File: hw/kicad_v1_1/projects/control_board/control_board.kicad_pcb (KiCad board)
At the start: 2 copper layers, 100 x 50 mm, 73 parts, among them CON1 161-0725-E, IC1 ATMEGA168A-A, P1 CONN_02X12_isolate_hv, P2 CONN_02X06, P3 CONN_02X05, P4 CONN_01X01, P5 CONN_01X01, P6 CONN_01X01, P7 CONN_01X01, Q1 IPB50R199CP, SW1 SW_LPH_PUSH, SW2 SW_LPH_PUSH, SW3 SW_LPH_PUSH, SW4 SW_LPH_PUSH, U1 MAX1771, U2 MCP7940N, U3 74HC595, U4 74HC595, U5 TPS563208, Y1 32.768kHz

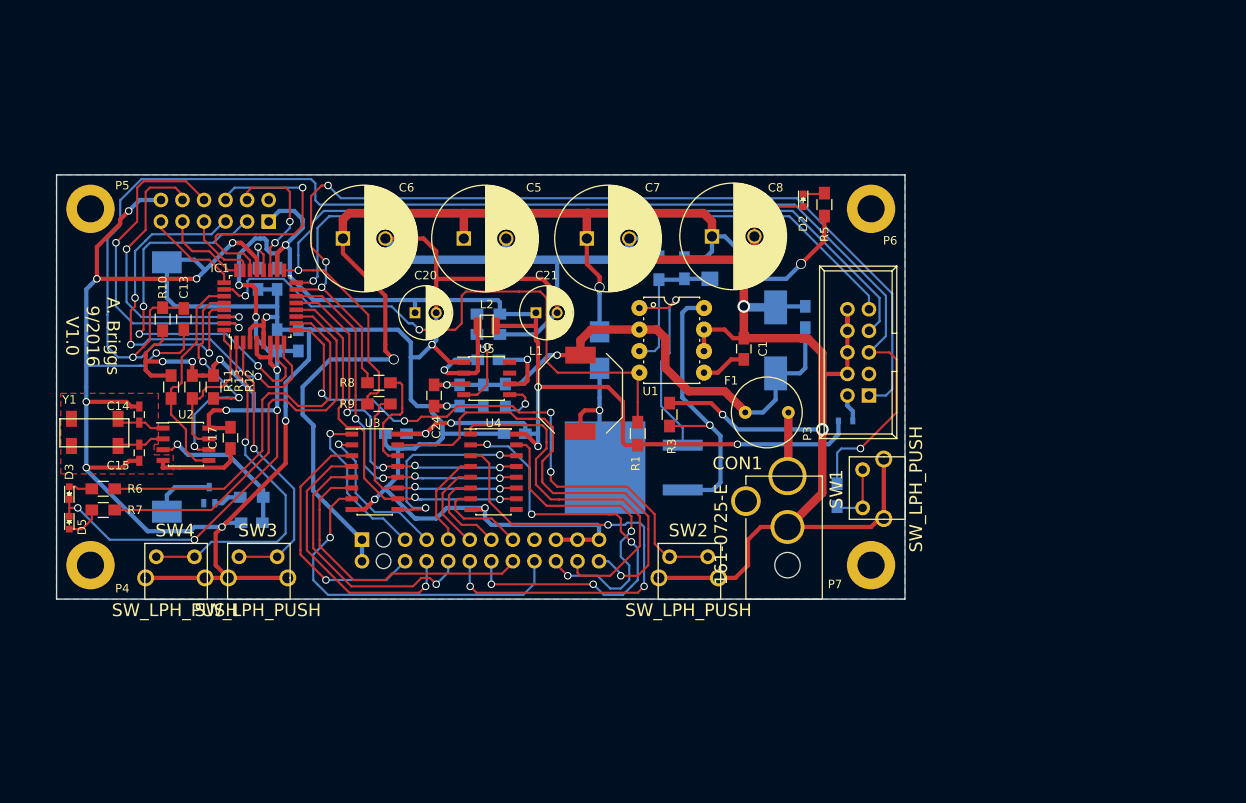
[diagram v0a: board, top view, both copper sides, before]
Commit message: Updates to BOM
Start to update BOM for 180V supply
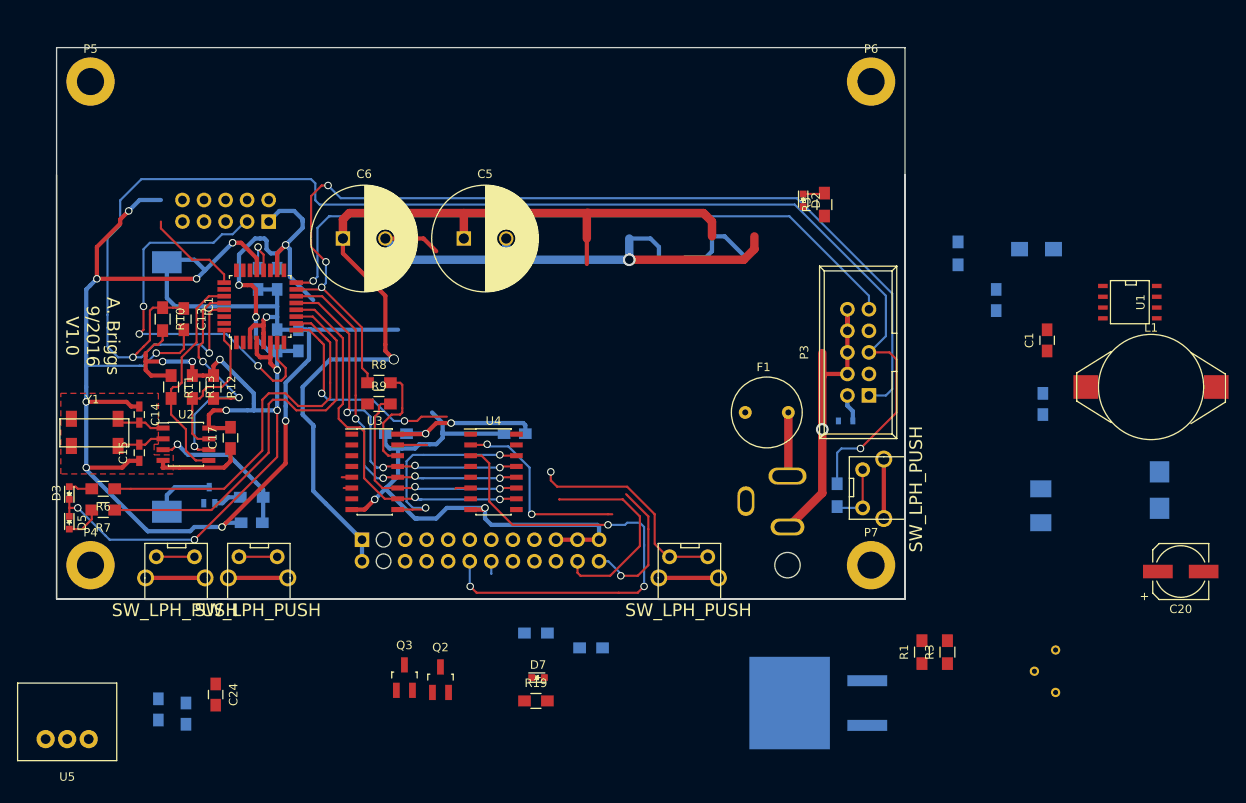
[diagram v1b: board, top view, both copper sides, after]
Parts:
- removed C21: 22uF, Capacitors_ThroughHole:C_Radial_D6.3_L11.2_P2.5
- removed C25: 0.1uF, Capacitors_SMD:C_0805_HandSoldering
- removed C7, C8: 47uF, Capacitors_ThroughHole:C_Radial_D12.5_L25_P5
- removed L2: LBR2518T2R2M, Nixie:ind_2518
- added D7: LTST-C190GKT, LEDs:LED_0603, F.Cu at (171.2, 129.2)
- added Q2: MMBTA42, TO_SOT_Packages_SMD:SOT-23_Handsoldering, F.Cu at (159.8, 129.5)
- added Q3: MMBTA42, TO_SOT_Packages_SMD:SOT-23_Handsoldering, F.Cu at (155.5, 129.2)
- added R19: 330, Resistors_SMD:R_0805_HandSoldering, F.Cu at (171.0, 132.0)
- C2: value 68uF -> 10uF; footprint Capacitors_Tantalum_SMD:TantalC_SizeD_EIA-7343_HandSoldering -> Capacitors_SMD:C_1210_HandSoldering
- C20: value 22uF -> 100uF; footprint Capacitors_ThroughHole:C_Radial_D6.3_L11.2_P2.5 -> Capacitors_SMD:c_elec_6.3x7.7
- CON1: moved to B.Cu
- L1: value 150u -> 100u; footprint Nixie:SRU1048-151Y -> Nixie:B82479A1104M
- P2: value CONN_02X06 -> CONN_02X05; footprint Pin_Headers:Pin_Header_Straight_2x06 -> Pin_Headers:Pin_Header_Straight_2x05
- R15: value 10k -> 4.7k
- R16: value 10k -> RVAR-TRIM; footprint Resistors_SMD:R_0805_HandSoldering -> Nixie:67ZR5KLF
- R17: value 33.2k -> 470k
- R3: value 0.1 -> 0.05
- R4: value 1.123MEG -> 1.5MEG
- R5: value 18k -> 1.5k
- R6, R7: value 100 -> 330
- U1: footprint Power_Integrations:PDIP-8 -> SMD_Packages:SOIC-8-N
- U5: value TPS563208 -> R-78E5.0-0.5; footprint Housings_SOIC:SOIC-8_3.9x4.9mm_Pitch1.27mm -> Nixie:R-78E5.0-0.5
- moved C20 95.3 mm to (247.0, 116.8)
- moved R16 72.5 mm to (232.2, 128.5)
- moved D1 68.0 mm to (244.5, 103.8)
- moved L1 67.3 mm to (243.5, 95.0), turned to 0 degrees
- moved U5 65.2 mm to (115.8, 136.5)
- moved U1 54.2 mm to (241.0, 85.0)
- moved C23 53.3 mm to (126.5, 133.0)
- moved C22 49.5 mm to (129.8, 133.5)
- moved C24 43.7 mm to (133.2, 131.2)
- moved R3 43.1 mm to (219.5, 126.2)
- moved R1 42.3 mm to (216.5, 126.2)
- moved R15 38.9 mm to (177.5, 125.8)
- moved R17 38.0 mm to (171.0, 124.0)
- moved C4 36.9 mm to (225.2, 84.8)
- moved C2 36.8 mm to (230.5, 109.0)
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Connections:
- net /MCU/SEL_DOT_BOT renamed /MCU/SEL_N2_D
- C10 pad 1: +3V3 -> +5V
- C11 pad 1: +3V3 -> +5V
- C17 pad 2: +3V3 -> +5V
- C18 pad 1: +3V3 -> +5V
- C19 pad 1: +3V3 -> +5V
- C20 pad 1: +3V3 -> +12V
- C22 pad 1: +12V -> +5V
- C4 pad 2: +170V -> +180V
- C5 pad 1: +170V -> +180V
- C6 pad 1: +170V -> +180V
- C9 pad 1: +3V3 -> +5V
- CON1 pad 2: Net-(CON1-Pad2) -> (no net)
- D1 pad 1: +170V -> +180V
- D2 pad 2: GND -> Net-(D2-Pad2)
- D3 pad 1: +3V3 -> +5V
- D4 pad 2: +3V3 -> +5V
- D5 pad 1: +3V3 -> +5V
- D6 pad 2: Net-(D6-Pad2) -> (no net)
- IC1 pad 18: +3V3 -> +5V
- IC1 pad 26: /Nixie Power Supply/180V_SHDN -> /MCU/180V_EN
- IC1 pad 4: +3V3 -> +5V
- IC1 pad 6: +3V3 -> +5V
- IC1 pad 8: /MCU/CYA1 -> /MCU/COL_SEL
- P1 pad 1: +170V -> +180V
- P1 pad 10: /MCU/SEL_FIVE -> /MCU/SEL_N2_C
- P1 pad 11: /MCU/SEL_NIX1 -> /MCU/SEL_N3_D
- P1 pad 13: /MCU/SEL_NIX2 -> /MCU/SEL_N0_A
- P1 pad 14: /MCU/SEL_DOT_TOP -> /MCU/SEL_N1_A
- P1 pad 15: /MCU/SEL_NIX3 -> /MCU/SEL_N0_B
- P1 pad 16: /MCU/SEL_SIX -> /MCU/SEL_N1_B
- P1 pad 17: Net-(P1-Pad17) -> /MCU/SEL_N0_C
- P1 pad 18: /MCU/SEL_SEVEN -> /MCU/SEL_N1_C
- P1 pad 19: GND -> /MCU/SEL_N0_D
- P1 pad 2: +170V -> +180V
- P1 pad 20: /MCU/SEL_EIGHT -> /MCU/SEL_N1_D
- P1 pad 21: GND -> +5V
- P1 pad 22: /MCU/SEL_NINE -> /MCU/COL_SEL
- P1 pad 24: /MCU/SEL_ZERO -> GND
- P1 pad 5: /MCU/SEL_ONE -> /MCU/SEL_N3_A
- P1 pad 6: /MCU/SEL_THREE -> /MCU/SEL_N2_A
- P1 pad 7: /MCU/SEL_TWO -> /MCU/SEL_N3_B
- P1 pad 8: /MCU/SEL_FOUR -> /MCU/SEL_N2_B
- P1 pad 9: /MCU/SEL_NIX0 -> /MCU/SEL_N3_C
- P2 pad 1: +3V3 -> +5V
- P2 pad 10: /MCU/CYA5 -> GND
- P2 pad 2: Net-(P2-Pad2) -> /MCU/CYA7
- P2 pad 4: /MCU/CYA7 -> /MCU/CYA8
- P2 pad 5: /MCU/CYA1 -> /MCU/CYA2
- P2 pad 6: /MCU/CYA8 -> /MCU/CYA6
- P2 pad 7: /MCU/CYA2 -> /MCU/CYA3
- P2 pad 8: /MCU/CYA6 -> /MCU/CYA5
- P2 pad 9: /MCU/CYA3 -> /MCU/CYA4
- P3 pad 3: Net-(P3-Pad3) -> (no net)
- P4 pad 1: Net-(P4-Pad1) -> (no net)
- P5 pad 1: Net-(P5-Pad1) -> (no net)
- P6 pad 1: Net-(P6-Pad1) -> (no net)
- P7 pad 1: Net-(P7-Pad1) -> (no net)
- R1 pad 1: +3V3 -> +12V
- R1 pad 2: /Nixie Power Supply/180V_SHDN -> Net-(Q2-Pad3)
- R10 pad 2: +3V3 -> +5V
- R11 pad 1: +3V3 -> +5V
- R12 pad 1: +3V3 -> +5V
- R13 pad 1: +3V3 -> +5V
- R15 pad 1: GND -> Net-(Q2-Pad1)
- R15 pad 2: Net-(R15-Pad2) -> /MCU/180V_EN
- R16 pad 1: Net-(R16-Pad1) -> Net-(C4-Pad1)
- R16 pad 2: +12V -> Net-(R16-Pad2)
- R17 pad 1: +3V3 -> Net-(Q3-Pad1)
- R17 pad 2: Net-(R15-Pad2) -> +180V
- R2 pad 1: Net-(C4-Pad1) -> Net-(R16-Pad2)
- R4 pad 2: +170V -> +180V
- R5 pad 1: +170V -> +12V
- SW1 pad 2: GND -> Net-(R18-Pad1)
- SW1 pad 3: Net-(R18-Pad1) -> (no net)
- SW1 pad 4: Net-(R18-Pad1) -> GND
- SW2 pad 2: GND -> Net-(IC1-Pad9)
- SW2 pad 3: Net-(IC1-Pad9) -> (no net)
- SW2 pad 4: Net-(IC1-Pad9) -> GND
- SW3 pad 2: GND -> Net-(IC1-Pad2)
- SW3 pad 3: Net-(IC1-Pad2) -> (no net)
- SW3 pad 4: Net-(IC1-Pad2) -> GND
- SW4 pad 2: GND -> Net-(IC1-Pad1)
- SW4 pad 3: Net-(IC1-Pad1) -> (no net)
- SW4 pad 4: Net-(IC1-Pad1) -> GND
- U1 pad 4: /Nixie Power Supply/180V_SHDN -> Net-(Q2-Pad3)
- U2 pad 8: +3V3 -> +5V
- U3 pad 1: /MCU/SEL_ONE -> /MCU/SEL_N0_B
- U3 pad 15: /MCU/SEL_ZERO -> /MCU/SEL_N0_A
- U3 pad 16: +3V3 -> +5V
- U3 pad 2: /MCU/SEL_TWO -> /MCU/SEL_N0_C
- U3 pad 3: /MCU/SEL_THREE -> /MCU/SEL_N0_D
- U3 pad 4: /MCU/SEL_FOUR -> /MCU/SEL_N1_A
- U3 pad 5: /MCU/SEL_FIVE -> /MCU/SEL_N1_B
- U3 pad 6: /MCU/SEL_SIX -> /MCU/SEL_N1_C
- U3 pad 7: /MCU/SEL_SEVEN -> /MCU/SEL_N1_D
- U4 pad 1: /MCU/SEL_NINE -> /MCU/SEL_N2_B
- U4 pad 15: /MCU/SEL_EIGHT -> /MCU/SEL_N2_A
- U4 pad 16: +3V3 -> +5V
- U4 pad 2: /MCU/SEL_DOT_TOP -> /MCU/SEL_N2_C
- U4 pad 4: /MCU/SEL_NIX0 -> /MCU/SEL_N3_A
- U4 pad 5: /MCU/SEL_NIX1 -> /MCU/SEL_N3_B
- U4 pad 6: /MCU/SEL_NIX2 -> /MCU/SEL_N3_C
- U4 pad 7: /MCU/SEL_NIX3 -> /MCU/SEL_N3_D
- U4 pad 9: Net-(U4-Pad9) -> (no net)
- U5 pad 1: GND -> +12V
- U5 pad 2: Net-(C25-Pad2) -> GND
- U5 pad 3: +12V -> +5V
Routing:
- net +3V3: track 257.5 -> 0.00 mm, vias 16 -> 0
- net GND: track 564.9 -> 394.2 mm, vias 18 -> 15
- net +5V: track 0.00 -> 161.0 mm, vias 0 -> 13
- net +170V: track 146.6 -> 0.00 mm, vias 3 -> 0
- net +180V: track 0.00 -> 110.7 mm, vias 0 -> 1
- net Net-(IC1-Pad17): track 106.6 -> 0.12 mm, vias 1 -> 0
- net /Nixie Power Supply/180V_SHDN: track 71.6 -> 0.00 mm, vias 2 -> 0
- net +12V: track 64.7 -> 0.00 mm, vias 2 -> 0
- net /MCU/SEL_ZERO: track 56.4 -> 0.00 mm, vias 1 -> 0
- net /MCU/SEL_DOT_TOP: track 54.2 -> 0.00 mm, vias 5 -> 0
- net /MCU/CYA1: track 50.0 -> 0.00 mm, vias 3 -> 0
- net /MCU/SEL_NINE: track 44.7 -> 0.00 mm
- net /MCU/SEL_SEVEN: track 42.3 -> 0.00 mm, vias 1 -> 0
- net /MCU/CYA6: track 41.7 -> 0.38 mm, vias 2 -> 0
- net /MCU/SEL_EIGHT: track 38.8 -> 0.00 mm, vias 2 -> 0
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- removed copper zone on B.Cu, net GND
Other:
- board size 100 x 50 mm -> 100 x 65 mm

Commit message: Complete with errors
Check in before moving header. Currently the headers don't match up. If
I'm going to connect them with standard header I need to move it
significantly. Check in as a roll back point.
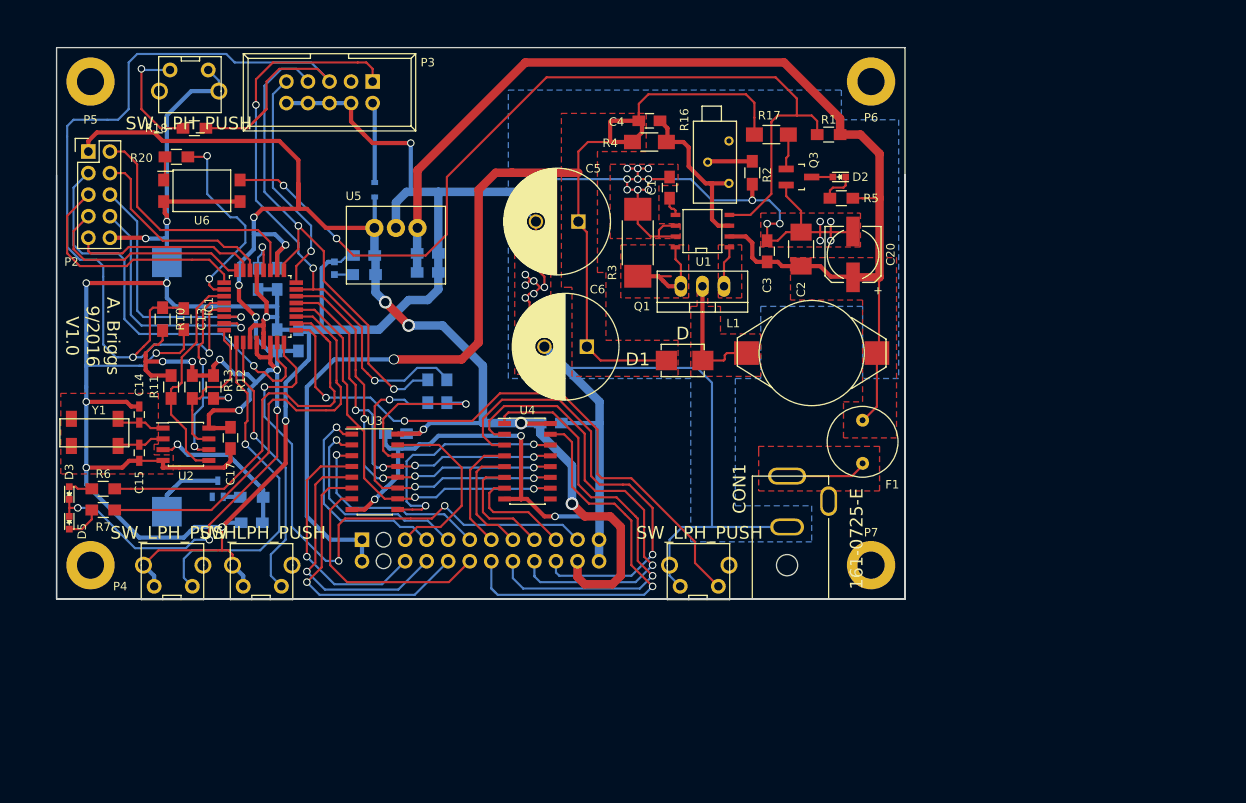
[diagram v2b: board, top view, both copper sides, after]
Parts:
- removed Q2: MMBTA42, TO_SOT_Packages_SMD:SOT-23_Handsoldering
- removed R15: 4.7k, Resistors_SMD:R_0805_HandSoldering
- added R20: 1k, Resistors_SMD:R_0805_HandSoldering, F.Cu at (128.6, 67.9)
- added U6: LTV-817, Opto-Devices:Optocoupler_SMD_LTV-817S, F.Cu at (131.6, 71.9)
- C2, C3, C4, CON1, D1, P2, R16, R18, R2, R4: moved to F.Cu
- C24, D7, R19, R8, R9: moved to B.Cu
- Q1: value IPB50R199CP -> IRF644PBF; footprint Nixie:to263 -> TO_SOT_Packages_THT:TO-220_Neutral123_Vertical; moved to F.Cu
- R17: footprint Resistors_SMD:R_0805_HandSoldering -> Resistors_SMD:R_1206_HandSoldering; moved to F.Cu
- R3: footprint Resistors_SMD:R_0805_HandSoldering -> Resistors_SMD:R_2512_HandSoldering
- moved SW1 91.3 mm to (132.4, 60.1), turned to 180 degrees
- moved R18 87.2 mm to (130.8, 64.5), turned to 0 degrees
- moved Q3 75.1 mm to (202.0, 70.2), turned to 270 degrees
- moved U5 71.6 mm to (154.5, 76.2), turned to 180 degrees
- moved R16 71.3 mm to (193.8, 68.5), turned to 270 degrees
- moved P3 69.2 mm to (151.8, 59.0), turned to 180 degrees
- moved R17 65.0 mm to (198.8, 65.2)
- moved R1 62.0 mm to (205.5, 65.2), turned to 180 degrees
- moved D4 61.8 mm to (152.0, 71.8), turned to 270 degrees
- moved D1 60.6 mm to (185.1, 91.9), turned to 0 degrees
- moved R3 60.5 mm to (183.0, 78.0)
- moved C23 60.5 mm to (158.2, 81.5), turned to 0 degrees
- moved C22 57.9 mm to (150.8, 79.5), turned to 180 degrees
- moved C24 57.7 mm to (158.2, 79.2), turned to 0 degrees
- moved R19 54.2 mm to (150.8, 81.8), turned to 180 degrees
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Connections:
- net Net-(Q2-Pad3) renamed /MCU/180V_SHDN
- IC1 pad 23: /MCU/CYA2 -> /MCU/CYA4
- IC1 pad 25: /MCU/CYA4 -> /MCU/CYA2
- IC1 pad 30: /MCU/CYA5 -> /MCU/CYA6
- IC1 pad 31: /MCU/CYA6 -> /MCU/CYA5
- IC1 pad 8: /MCU/COL_SEL -> /SEL_COL
- P1 pad 10: /MCU/SEL_N2_C -> /SEL_N3_C
- P1 pad 11: /MCU/SEL_N3_D -> /SEL_N2_D
- P1 pad 12: /MCU/SEL_N2_D -> /SEL_N3_D
- P1 pad 13: /MCU/SEL_N0_A -> /SEL_N1_A
- P1 pad 14: /MCU/SEL_N1_A -> /SEL_N0_A
- P1 pad 15: /MCU/SEL_N0_B -> /SEL_N1_B
- P1 pad 16: /MCU/SEL_N1_B -> /SEL_N0_B
- P1 pad 17: /MCU/SEL_N0_C -> /SEL_N1_C
- P1 pad 18: /MCU/SEL_N1_C -> /SEL_N0_C
- P1 pad 19: /MCU/SEL_N0_D -> /SEL_N1_D
- P1 pad 20: /MCU/SEL_N1_D -> /SEL_N0_D
- P1 pad 21: +5V -> /SEL_COL
- P1 pad 22: /MCU/COL_SEL -> +5V
- P1 pad 5: /MCU/SEL_N3_A -> /SEL_N2_A
- P1 pad 6: /MCU/SEL_N2_A -> /SEL_N3_A
- P1 pad 7: /MCU/SEL_N3_B -> /SEL_N2_B
- P1 pad 8: /MCU/SEL_N2_B -> /SEL_N3_B
- P1 pad 9: /MCU/SEL_N3_C -> /SEL_N2_C
- U3 pad 1: /MCU/SEL_N0_B -> /SEL_N2_B
- U3 pad 15: /MCU/SEL_N0_A -> /SEL_N2_A
- U3 pad 2: /MCU/SEL_N0_C -> /SEL_N2_C
- U3 pad 3: /MCU/SEL_N0_D -> /SEL_N2_D
- U3 pad 4: /MCU/SEL_N1_A -> /SEL_N3_A
- U3 pad 5: /MCU/SEL_N1_B -> /SEL_N3_B
- U3 pad 6: /MCU/SEL_N1_C -> /SEL_N3_C
- U3 pad 7: /MCU/SEL_N1_D -> /SEL_N3_D
- U4 pad 1: /MCU/SEL_N2_B -> /SEL_N0_B
- U4 pad 15: /MCU/SEL_N2_A -> /SEL_N0_A
- U4 pad 2: /MCU/SEL_N2_C -> /SEL_N0_C
- U4 pad 3: /MCU/SEL_N2_D -> /SEL_N0_D
- U4 pad 4: /MCU/SEL_N3_A -> /SEL_N1_A
- U4 pad 5: /MCU/SEL_N3_B -> /SEL_N1_B
- U4 pad 6: /MCU/SEL_N3_C -> /SEL_N1_C
- U4 pad 7: /MCU/SEL_N3_D -> /SEL_N1_D
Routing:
- net GND: track 394.2 -> 568.8 mm, vias 15 -> 36
- net +5V: track 161.0 -> 301.7 mm, vias 13 -> 17
- net +12V: track 0.00 -> 137.0 mm
- net /MCU/180V_SHDN: track 0.00 -> 107.1 mm, vias 0 -> 2
- net /SEL_COL: track 0.00 -> 69.3 mm, vias 0 -> 3
- net Net-(IC1-Pad17): track 0.12 -> 59.1 mm, vias 0 -> 2
- net /MCU/SEL_N2_D: track 58.1 -> 0.00 mm, vias 3 -> 0
- net Net-(C13-Pad1): track 176.7 -> 121.3 mm, vias 3 -> 2
- net /SEL_N0_C: track 0.00 -> 54.0 mm, vias 0 -> 1
- net /SEL_N0_D: track 0.00 -> 53.7 mm, vias 0 -> 1
- net Net-(IC1-Pad16): track 79.6 -> 27.0 mm
- net /SEL_N0_B: track 0.00 -> 52.2 mm, vias 0 -> 1
- net /SEL_N0_A: track 0.00 -> 49.3 mm, vias 0 -> 1
- net Net-(IC1-Pad15): track 116.9 -> 70.2 mm
- net +180V: track 110.7 -> 153.8 mm
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- added copper zone on F.Cu, net +12V
- added copper zone on F.Cu, net +180V
- added copper zone on B.Cu, net GND
- added copper zone on F.Cu, net Net-(CON1-Pad1)
- added copper zone on F.Cu, net Net-(D1-Pad2)
- added copper zone on F.Cu, net Net-(Q1-Pad1)
- added copper zone on F.Cu, net Net-(Q1-Pad3)

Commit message: Final Release
Update with trimming and bug fixes. This is what is being delivered as a
V1.1.0 release.
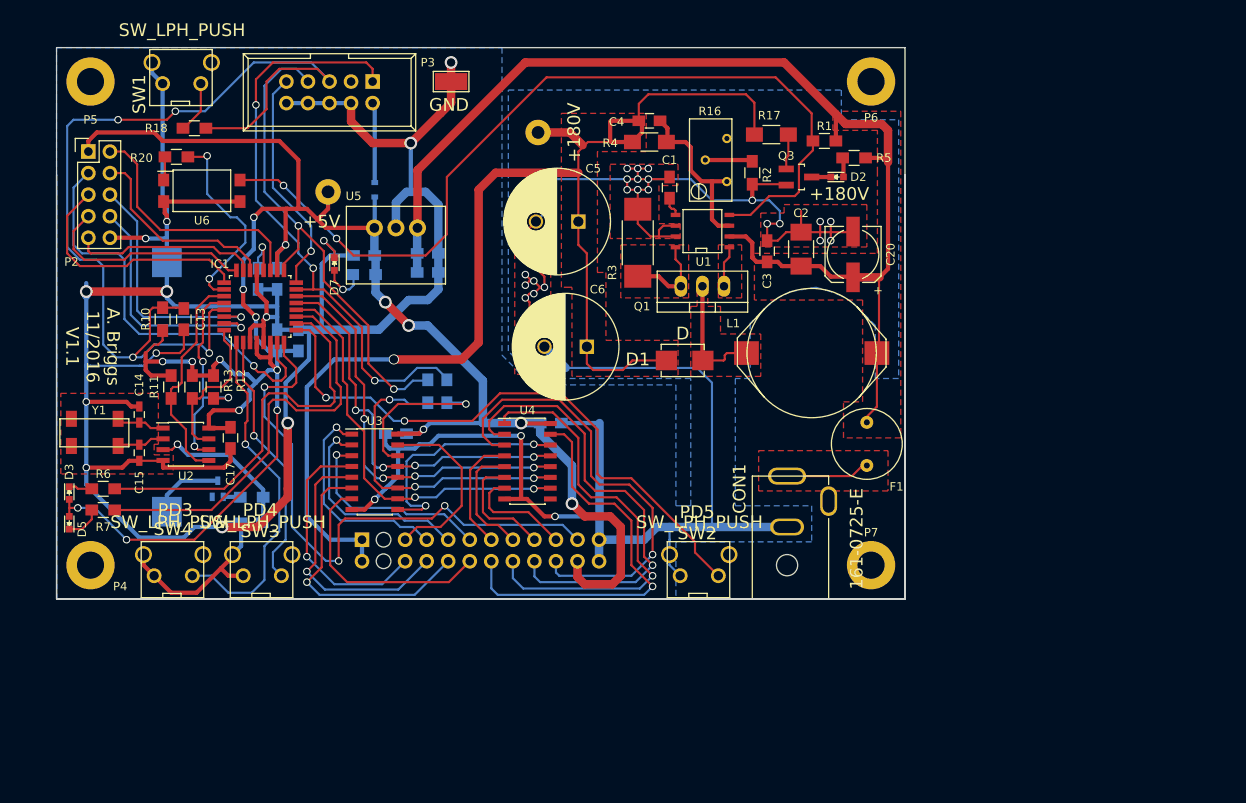
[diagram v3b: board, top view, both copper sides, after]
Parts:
- added W1: TEST_1P, Measurement_Points:Measurement_Point_Round-TH_Big, F.Cu at (171.2, 65.0)
- added W2: TEST_1P, Measurement_Points:Measurement_Point_Round-TH_Big, B.Cu at (146.5, 72.0)
- added W3: TEST_1P, Measurement_Points:Test_Point_Keystone_5019_Minature, F.Cu at (161.0, 59.0)
- D7: moved to F.Cu
- moved SW1 6.35 mm to (127.0, 56.8), turned to 0 degrees
- moved R5 4.98 mm to (208.5, 68.0)
- moved SW2 1.25 mm to (188.0, 114.8)
- moved SW3 1.25 mm to (136.5, 114.8)
- moved SW4 1.25 mm to (126.0, 114.8)
- moved R1 0.90 mm to (205.0, 66.0)
- moved F1 0.56 mm to (210.0, 104.2)
- moved D7 0.50 mm to (147.2, 80.5), turned to 270 degrees
- moved R16 0.35 mm to (193.5, 68.2), turned to 90 degrees
- moved D2 0.25 mm to (206.5, 70.2), turned to 0 degrees
- turned D3 to 270 degrees
- turned D5 to 90 degrees
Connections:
- D3 pad 1: +5V -> Net-(D3-Pad1)
- D3 pad 2: Net-(D3-Pad2) -> +5V
- D5 pad 1: +5V -> Net-(D5-Pad1)
- D5 pad 2: Net-(D5-Pad2) -> +5V
- D7 pad 1: Net-(D7-Pad1) -> GND
- D7 pad 2: GND -> Net-(D7-Pad2)
- Q3 pad 3: Net-(D2-Pad2) -> Net-(D2-Pad1)
- R19 pad 2: Net-(D7-Pad1) -> Net-(D7-Pad2)
- R5 pad 2: Net-(D2-Pad1) -> Net-(D2-Pad2)
- R6 pad 2: Net-(D3-Pad2) -> Net-(D3-Pad1)
- R7 pad 2: Net-(D5-Pad2) -> Net-(D5-Pad1)
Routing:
- net GND: track 568.8 -> 594.4 mm, vias 36 -> 38
- net +5V: track 301.7 -> 286.0 mm
- net +180V: track 153.8 -> 167.0 mm
- net Net-(R18-Pad1): track 14.0 -> 6.19 mm, vias 1 -> 0
- net Net-(C13-Pad1): track 121.3 -> 115.0 mm, vias 2 -> 4
- net Net-(D7-Pad2): track 0.00 -> 5.41 mm, vias 0 -> 1
- net Net-(D5-Pad2): track 4.23 -> 0.00 mm
- net Net-(D5-Pad1): track 0.00 -> 4.23 mm
- net Net-(Q1-Pad3): track 14.3 -> 10.4 mm
- net +12V: track 137.0 -> 140.8 mm
- net Net-(D3-Pad2): track 2.75 -> 0.00 mm
- net Net-(D3-Pad1): track 0.00 -> 2.75 mm
- net /MCU/180V_SHDN: track 107.1 -> 104.8 mm
- net Net-(D7-Pad1): track 2.15 -> 0.00 mm
- net Net-(D2-Pad1): track 4.00 -> 2.25 mm
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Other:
- board text added: "+180V"
- board text added: "+5V"
- board text added: "A. Briggs 11/2016 V1.1"
- board text added: "GND"
- board text added: "PD3"
- board text added: "PD4"
- board text added: "PD5"
- board text added: "PD6"
- board text added: "PD7"
- board text removed: "A. Briggs 9/2016 V1.0"
